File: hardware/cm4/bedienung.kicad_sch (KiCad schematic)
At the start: 9 parts, among them SW1 Taste

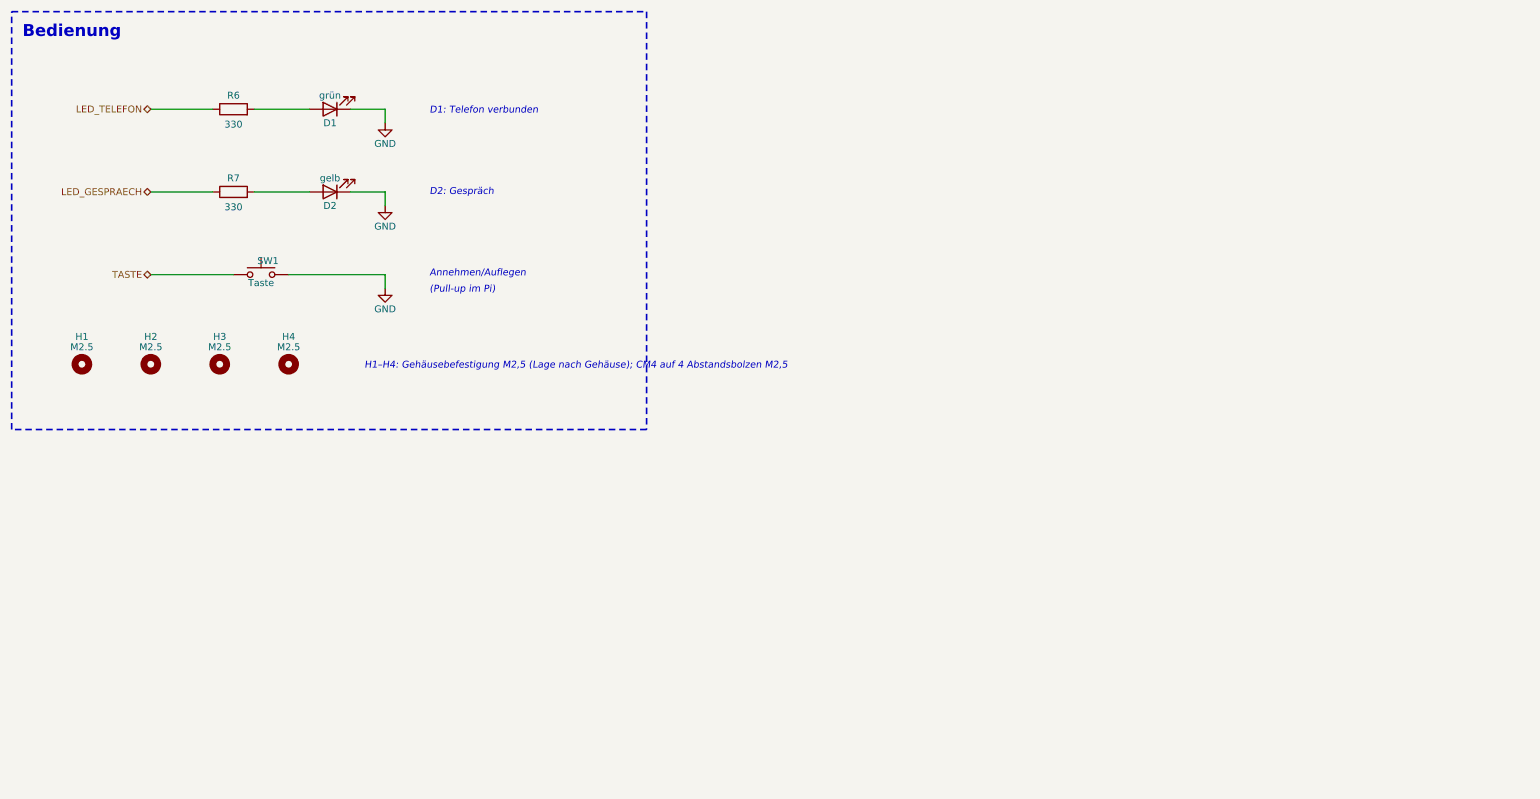
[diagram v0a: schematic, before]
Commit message: CM4-Schaltplan: Einzelblock-Blätter ohne Rahmen, Inhalt zentriert
kicadgen: Steht nur ein Block auf einem Blatt, entfällt der Rahmen (sein Titel wird
Blatttitel) und der Inhalt wird auf dem Blatt zentriert (über dem Schriftfeld, auf dem
1,27-mm-Raster). Hinweistexte der CM4-Blätter an die Schaltungen gerückt.

Co-Authored-By: Claude Opus 5.5 <noreply@anthropic.com>
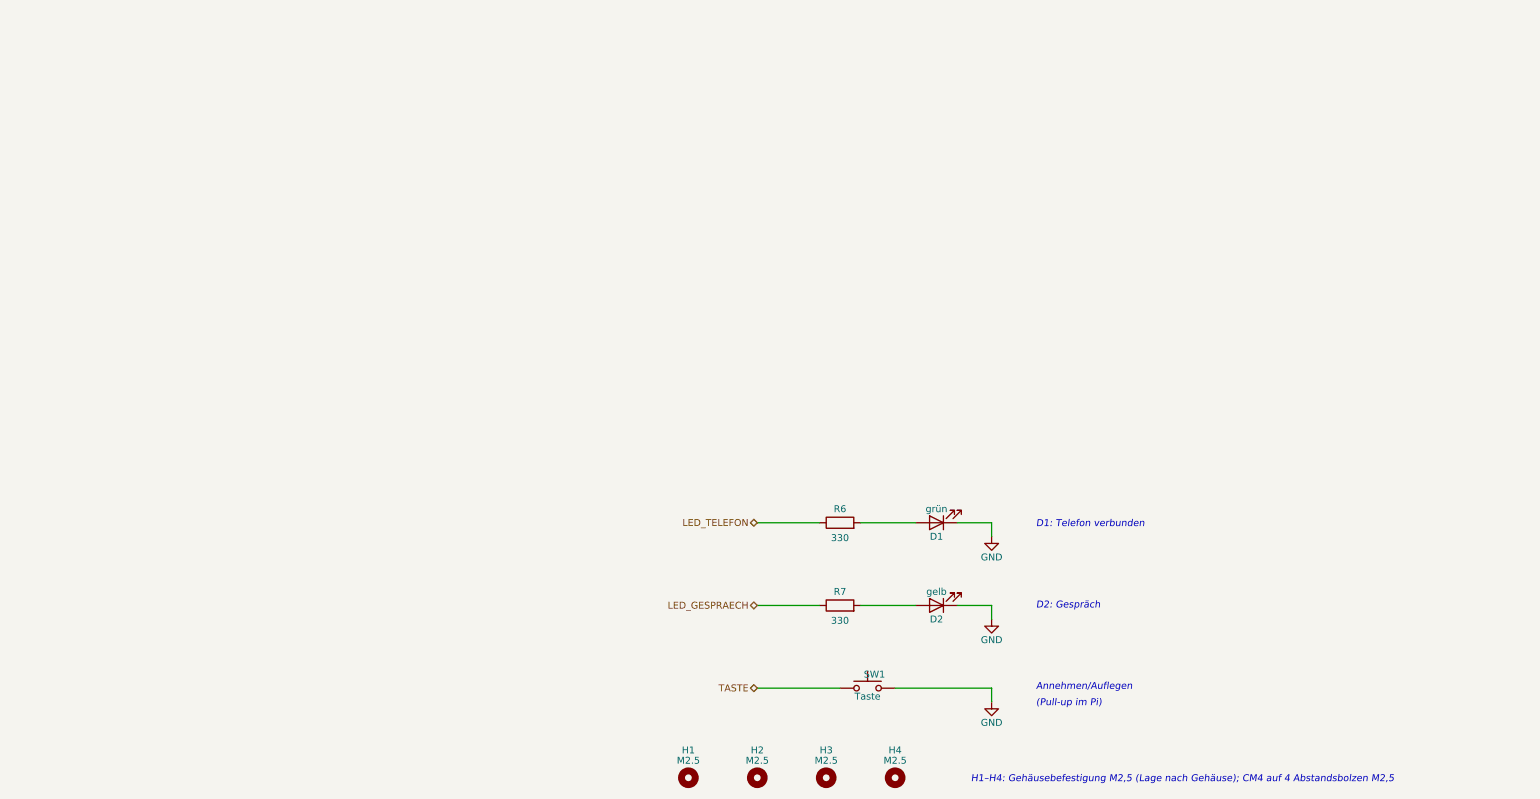
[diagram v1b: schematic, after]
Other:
- note removed: "Bedienung"
